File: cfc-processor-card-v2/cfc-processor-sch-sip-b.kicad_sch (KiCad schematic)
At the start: 33 parts, among them U7 OSD3358-1G-ISM, Y1 ECS-240-12-30BQ-AEN-TR, Y2 ABS07-32.768KHZ-T

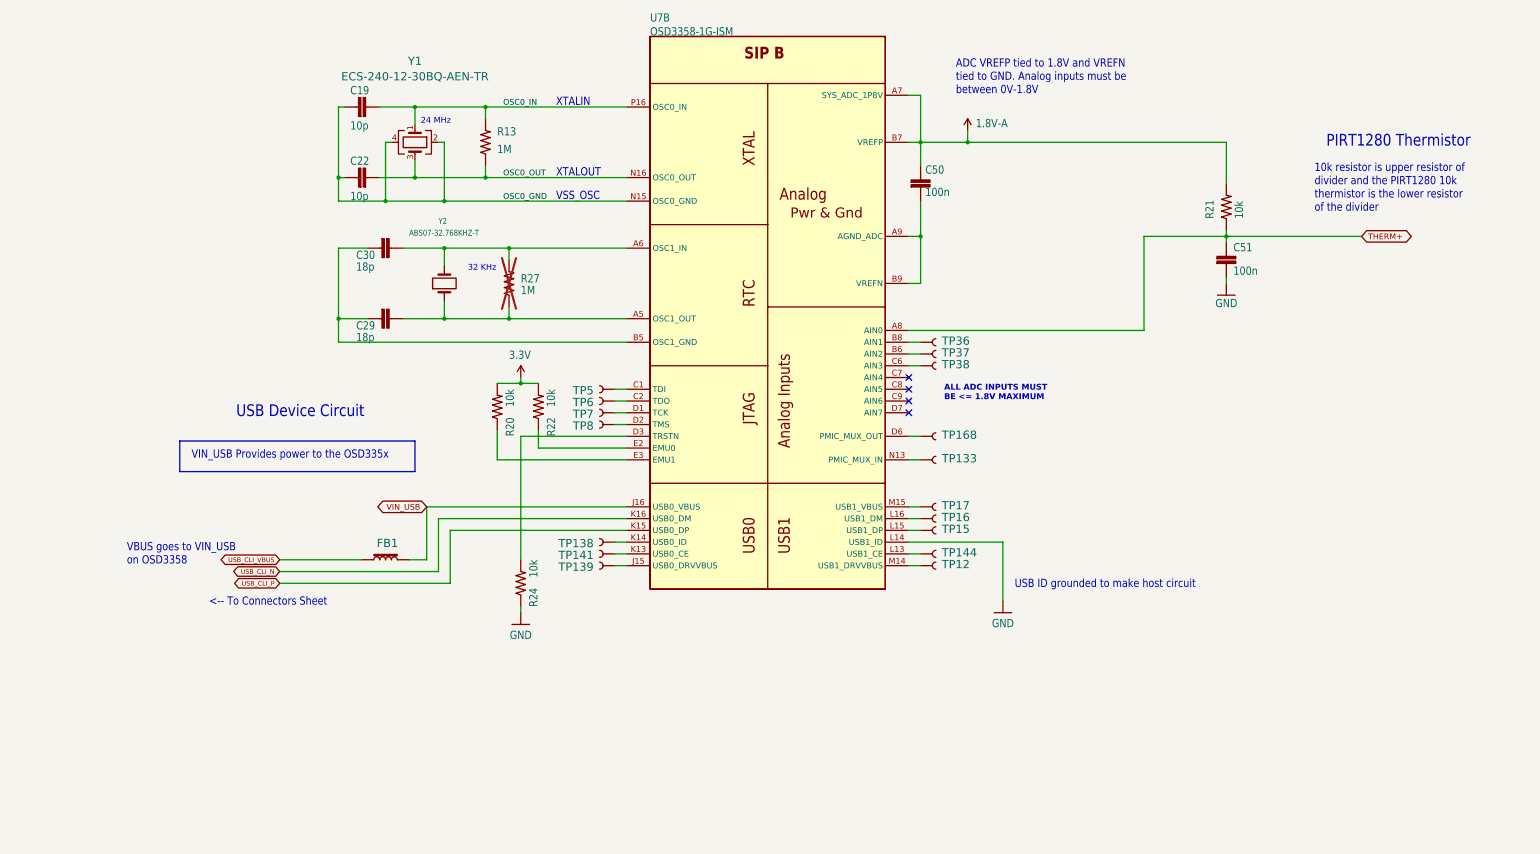
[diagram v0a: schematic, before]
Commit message: CFC processor schematic Change
changed to hierarchy view, changed all global net labels to hierarchy labels, changed all resistor, capacitor, and ground symbols to modern oresat labels. Deleted connectors sheet and added .history to gitignore.
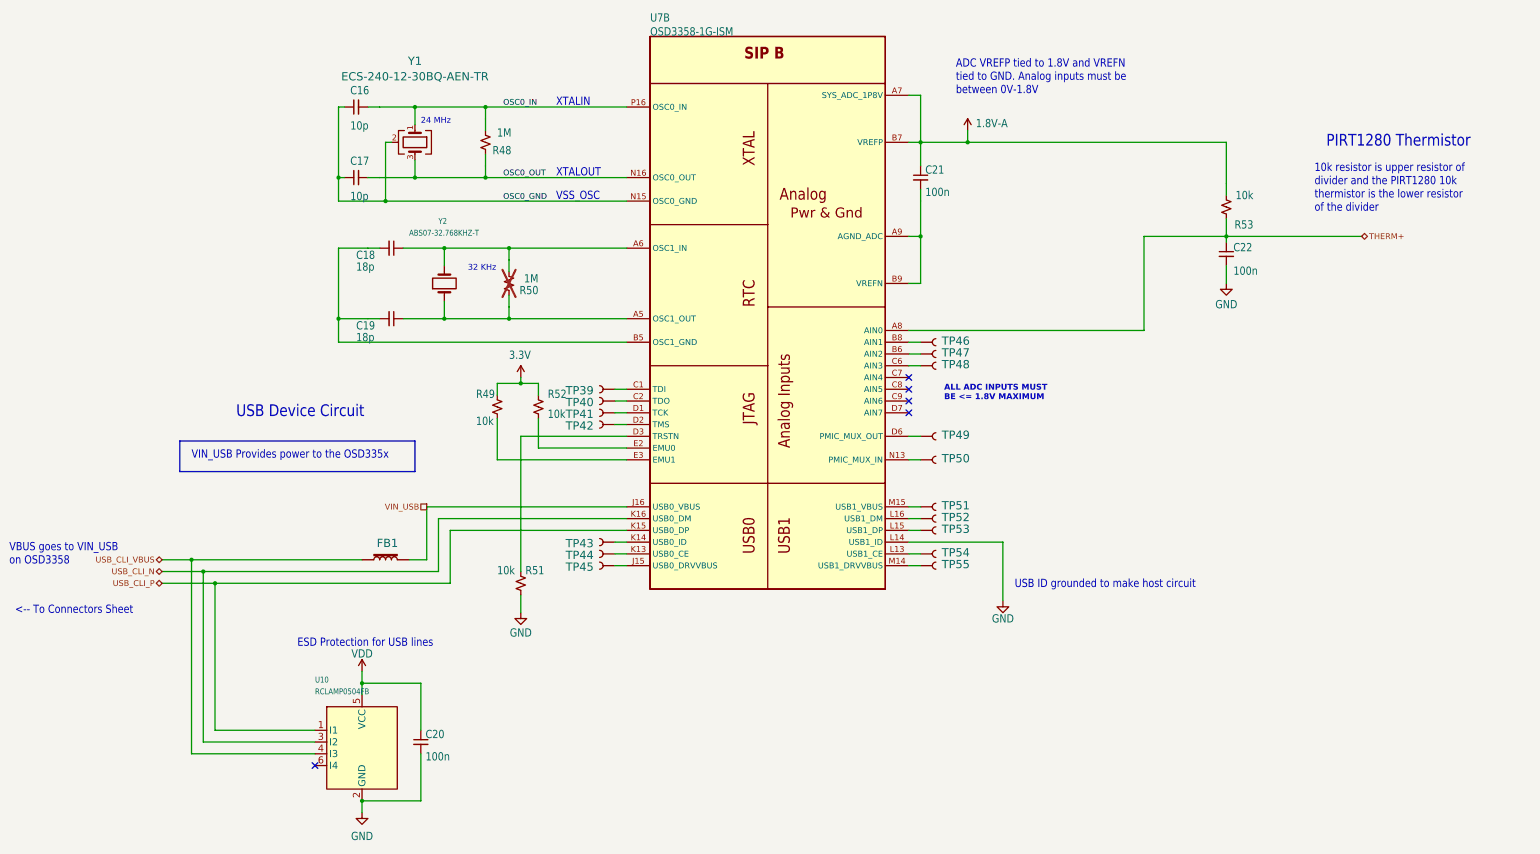
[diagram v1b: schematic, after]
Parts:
- added C20: 100n, oresat-passives:0603-C-NOSILK, symbol Device:C_Small
- added U10: RCLAMP0504FB, cfc-card:SC70-6, symbol cfc-card-eagle-import:RCLAMP0504FB
- C16: renamed from C19; symbol cfc-card-eagle-import:C-EU0603-A -> Device:C_Small
- C17: renamed from C22; symbol cfc-card-eagle-import:C-EU0603-A -> Device:C_Small
- C18: renamed from C30; symbol cfc-card-eagle-import:C-EU0603-A -> Device:C_Small
- C19: renamed from C29; symbol cfc-card-eagle-import:C-EU0603-A -> Device:C_Small
- C21: renamed from C50; symbol cfc-card-eagle-import:C-EU0603-A -> Device:C_Small
- C22: renamed from C51; symbol cfc-card-eagle-import:C-EU0603-A -> Device:C_Small
- R48: renamed from R13; symbol cfc-card-eagle-import:R-US_0603-A -> Device:R_Small_US
- R49: renamed from R20; symbol cfc-card-eagle-import:R-US_0603-A -> Device:R_Small_US
- R50: renamed from R27; symbol cfc-card-eagle-import:R-US_0603-A -> Device:R_Small_US
- R51: renamed from R24; symbol cfc-card-eagle-import:R-US_0603-A -> Device:R_Small_US
- R52: renamed from R22; symbol cfc-card-eagle-import:R-US_0603-A -> Device:R_Small_US
- R53: renamed from R21; symbol cfc-card-eagle-import:R-US_0603-A -> Device:R_Small_US
- renumbered TP5 to TP39, TP6 to TP40, TP7 to TP41, TP8 to TP42, TP138 to TP43, TP141 to TP44, TP139 to TP45, TP36 to TP46, TP37 to TP47, TP38 to TP48, TP168 to TP49, TP133 to TP50, TP17 to TP51, TP16 to TP52, TP15 to TP53, TP144 to TP54, TP12 to TP55
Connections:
- net GND: now also C20.2, U10.2 (GND)
- net USB_CLI_N: now also U10.3 (I2)
- net USB_CLI_P: now also U10.1 (I1)
- net USB_CLI_VBUS: now also U10.4 (I3)
- new net VDD: C20.1, U10.5 (VCC)
- no-connect marks 4 -> 5
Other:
- note added: "ESD Protection for USB lines"

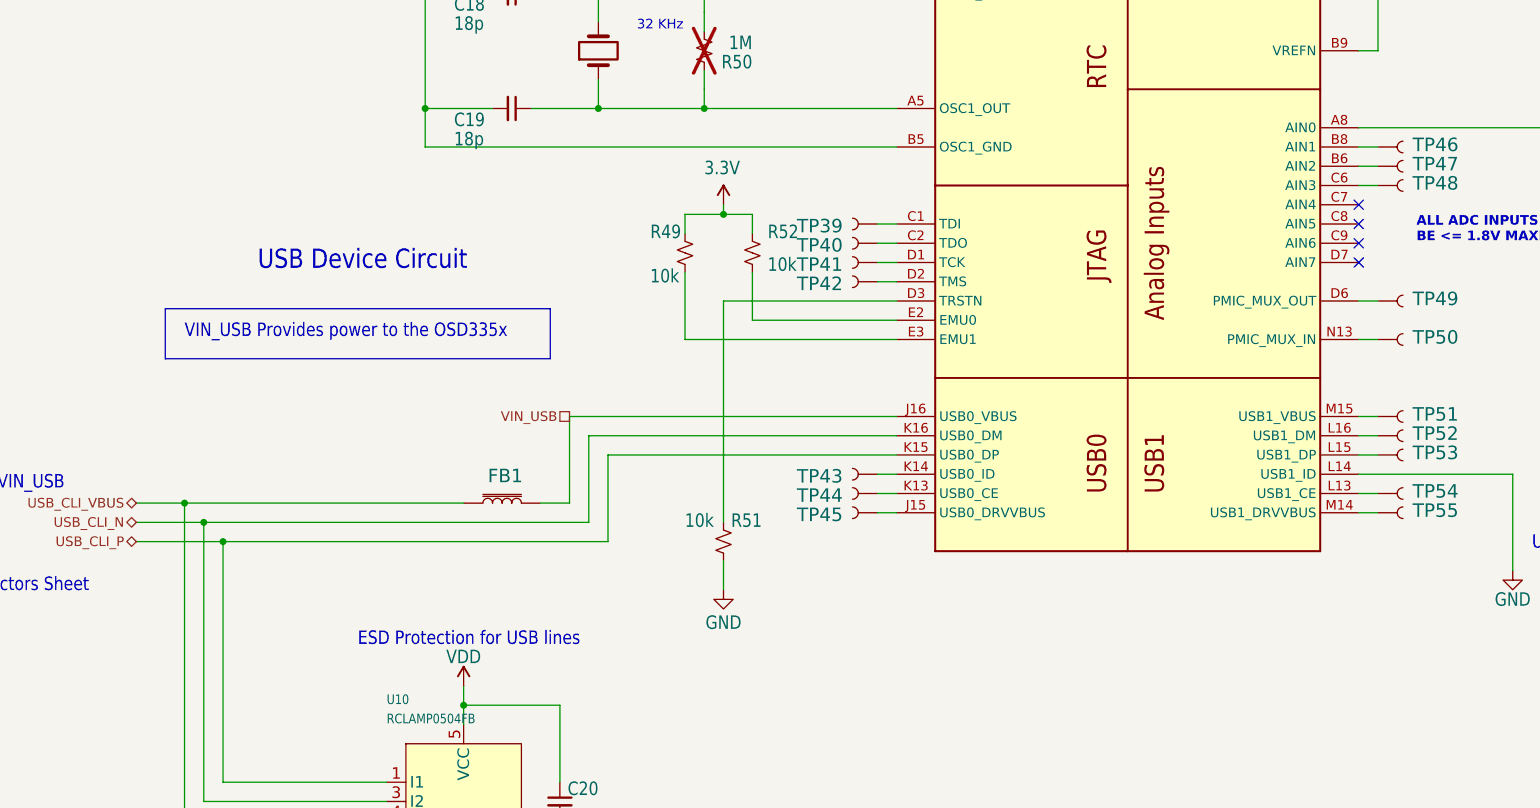
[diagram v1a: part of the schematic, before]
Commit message: Updated OPD
couple of resistors and caps added to schematic. Changed USB ESD clamp VDD to 3.3v instead of octavo created VDD line.
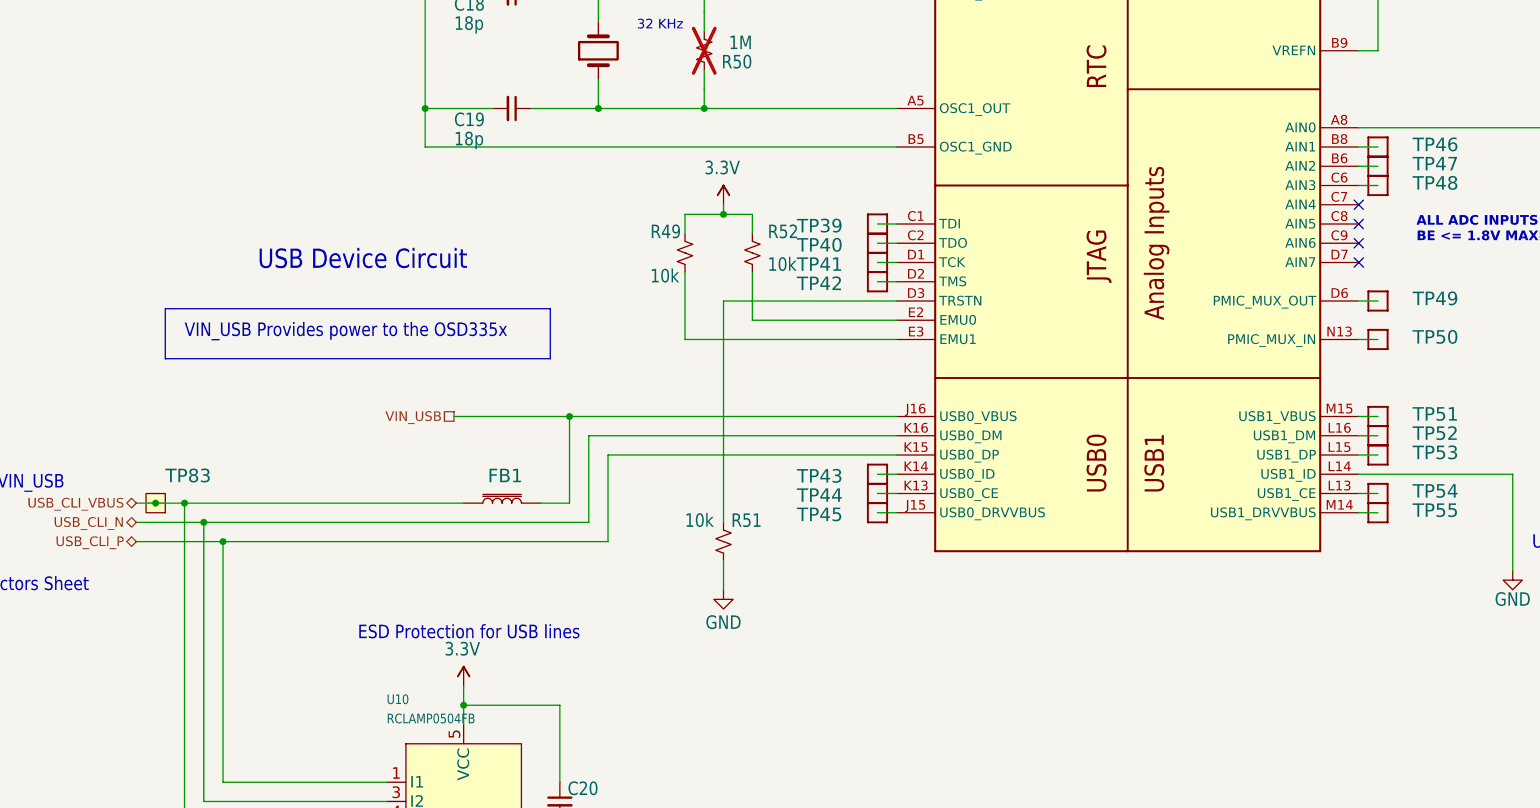
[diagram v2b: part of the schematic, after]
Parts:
- added TP83: TEST-POINT, oresat-misc:TestPoint-0.75mm-th, symbol Oresat Misc:Test-Point-0.75mm-th
- TP39, TP40, TP41, TP42, TP43, TP44, TP45, TP46, TP47, TP48, TP49, TP50, TP51, TP52, TP53, TP54, TP55: footprint cfc-card:PAD.03X.04 -> oresat-misc:TestPoint_Pad_D1.0mm; symbol cfc-card-eagle-import:TEST-POINT3X4 -> Oresat Misc:Test-Point-1mm-round
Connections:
- net VDD is gone; now on net 3.3V: C20.1, U10.5 (VCC)
- net USB_CLI_VBUS: now also TP83.1
- net at U7.D1 (TCK): now also TP41.1; no longer TP41.P$1 (1)
- net at U7.L16 (USB1_DM): now also TP52.1; no longer TP52.P$1 (1)
- net at U7.K14 (USB0_ID): now also TP43.1; no longer TP43.P$1 (1)
- net at U7.M15 (USB1_VBUS): now also TP51.1; no longer TP51.P$1 (1)
- net at U7.B6 (AIN2): now also TP47.1; no longer TP47.P$1 (1)
- net at U7.M14 (USB1_DRVVBUS): now also TP55.1; no longer TP55.P$1 (1)
- net at U7.B8 (AIN1): now also TP46.1; no longer TP46.P$1 (1)
- net at U7.N13 (PMIC_MUX_IN): now also TP50.1; no longer TP50.P$1 (1)
- net at U7.L15 (USB1_DP): now also TP53.1; no longer TP53.P$1 (1)
- net at U7.C6 (AIN3): now also TP48.1; no longer TP48.P$1 (1)
- net at U7.D2 (TMS): now also TP42.1; no longer TP42.P$1 (1)
- net at U7.K13 (USB0_CE): now also TP44.1; no longer TP44.P$1 (1)
- net at U7.C2 (TDO): now also TP40.1; no longer TP40.P$1 (1)
- net at U7.C1 (TDI): now also TP39.1; no longer TP39.P$1 (1)
- net at U7.L13 (USB1_CE): now also TP54.1; no longer TP54.P$1 (1)
- net at U7.D6 (PMIC_MUX_OUT): now also TP49.1; no longer TP49.P$1 (1)
- net at U7.J15 (USB0_DRVVBUS): now also TP45.1; no longer TP45.P$1 (1)

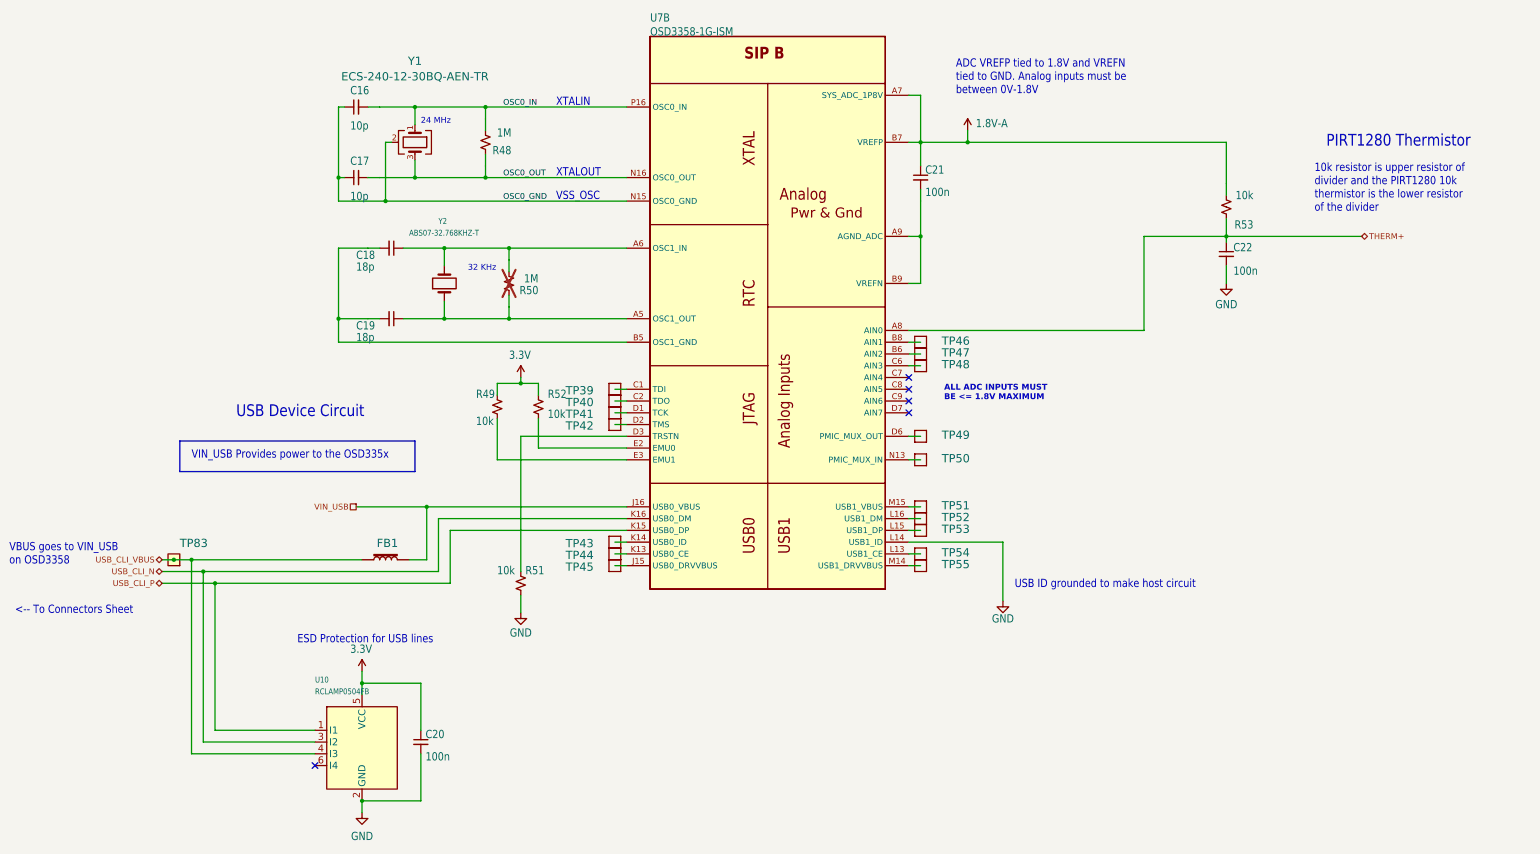
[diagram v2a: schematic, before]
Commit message: Update
Added pull down resistors and removed therm + and sensor enable and added i2c support for cfc sensor card.
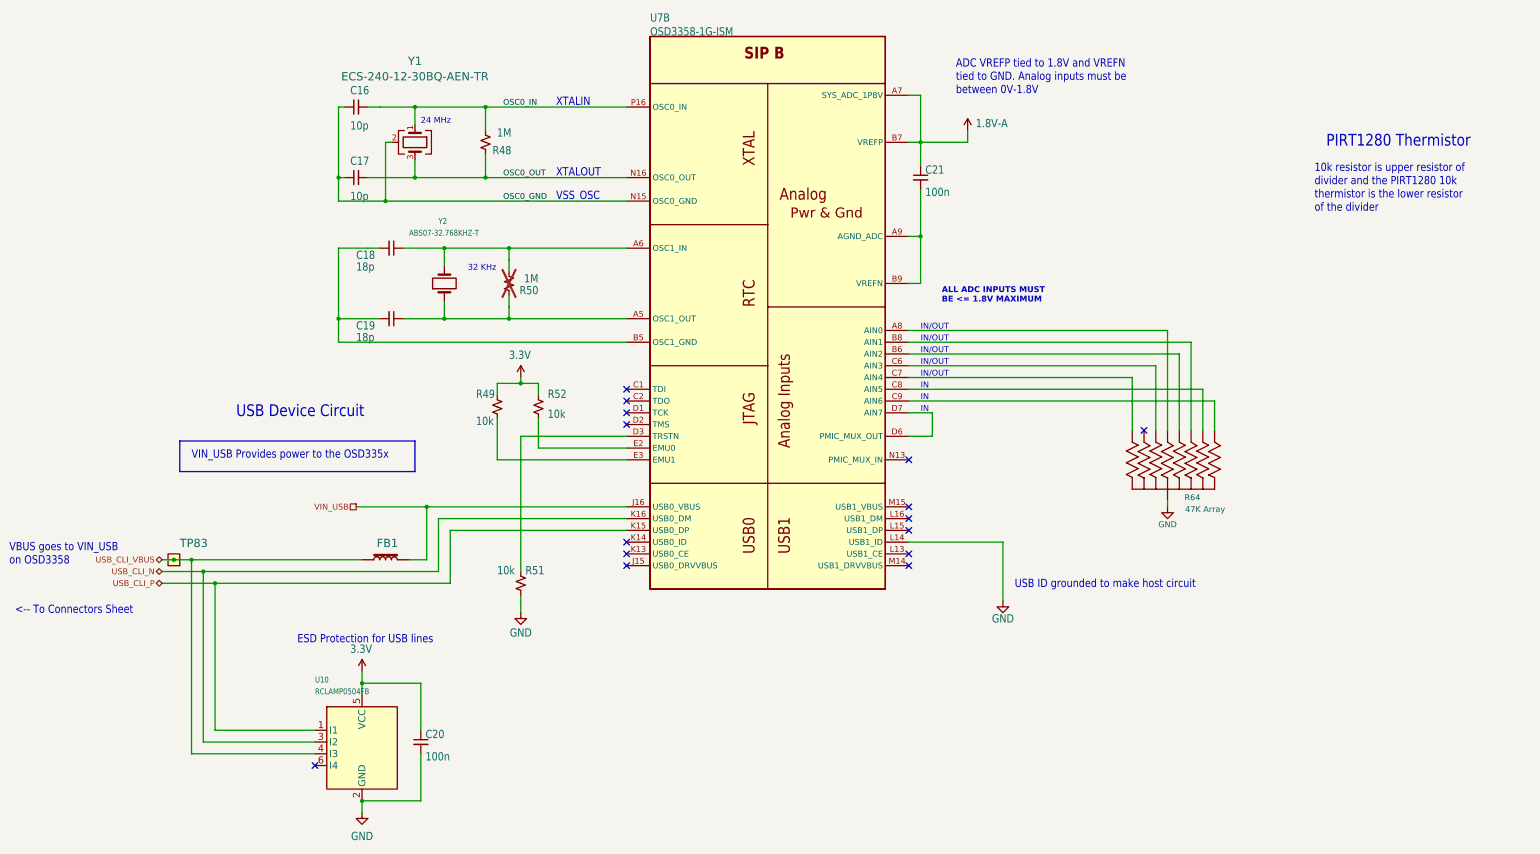
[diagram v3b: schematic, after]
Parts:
- removed C22: 100n, oresat-passives:0603-C-NOSILK, symbol Device:C_Small
- removed R53: 10k, oresat-passives:0603-C-NOSILK, symbol Device:R_Small_US
- removed TP39, TP40, TP41, TP42, TP43, TP44, TP45, TP46, TP47, TP48, TP49, TP50, TP51, TP52, TP53, TP54, TP55: TEST-POINT3X4, oresat-misc:TestPoint_Pad_D1.0mm, symbol Oresat Misc:Test-Point-1mm-round
- added R64: 47K Array, cfc-card:ARRAY_EXBA-M, symbol cfc-card-eagle-import:EXB-A10P391JC_ARRAY_EXBA-M
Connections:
- net GND: now also R64.10 (55), R64.5 (55)
- net at U7.B6 (AIN2): now also R64.8 (88)
- net at U7.B8 (AIN1): now also R64.2 (22)
- net at U7.C6 (AIN3): now also R64.7 (77)
- net at U7.D6 (PMIC_MUX_OUT): now also U7.D7 (AIN7)
- net at U7.C7 (AIN4): now also R64.6 (66)
- net at U7.C8 (AIN5): now also R64.9 (99)
- net at U7.C9 (AIN6): now also R64.1 (11)
- net THERM+: no longer names the net of U7.A8 (AIN0)
- net THERM+: now also R64.3 (33)
- no-connect marks 5 -> 15
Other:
- note added: "IN"
- note added: "IN/OUT"
